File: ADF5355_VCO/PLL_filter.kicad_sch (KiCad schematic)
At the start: 0 parts

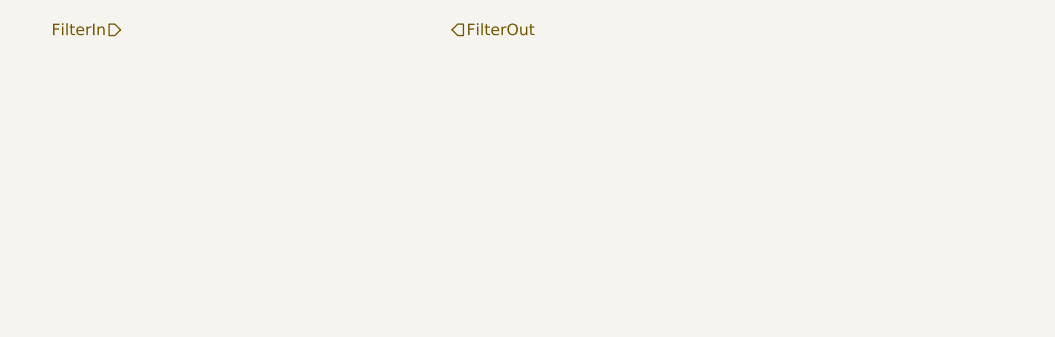
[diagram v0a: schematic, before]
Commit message: Added PLL filter
Added components for the PLL filter
 according to the components on evaluation board

Added specific components to BOM
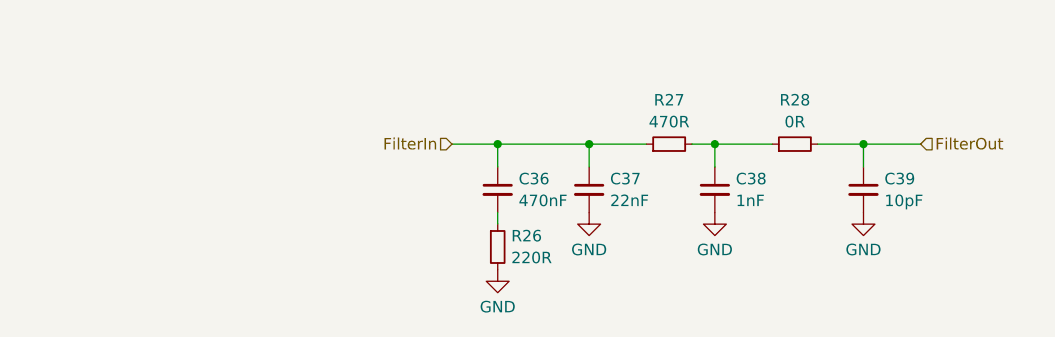
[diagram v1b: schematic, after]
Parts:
- added C36: 470nF, Capacitor_SMD:C_0603_1608Metric_Pad1.08x0.95mm_HandSolder, symbol Device:C_Small
- added C37: 22nF, Capacitor_SMD:C_0603_1608Metric_Pad1.08x0.95mm_HandSolder, symbol Device:C_Small
- added C38: 1nF, Capacitor_SMD:C_0603_1608Metric_Pad1.08x0.95mm_HandSolder, symbol Device:C_Small
- added C39: 10pF, Capacitor_SMD:C_0603_1608Metric_Pad1.08x0.95mm_HandSolder, symbol Device:C_Small
- added R26: 220R, Capacitor_SMD:C_0603_1608Metric_Pad1.08x0.95mm_HandSolder, symbol Device:R_Small
- added R27: 470R, Capacitor_SMD:C_0603_1608Metric_Pad1.08x0.95mm_HandSolder, symbol Device:R_Small
- added R28: 0R, Capacitor_SMD:C_0603_1608Metric_Pad1.08x0.95mm_HandSolder, symbol Device:R_Small
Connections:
- net FilterIn: now also C36.1, C37.1, R27.1
- net FilterOut: now also C39.1, R28.2
- new net: C36.2, R26.1
- new net: C38.1, R27.2, R28.1
- new net GND: C37.2, C38.2, C39.2, R26.2
